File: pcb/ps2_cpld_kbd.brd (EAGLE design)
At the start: 53 x 62.2 mm, 34 parts, among them J1 AVR ISP, J2 JTAG, J3 Emulated Mechanical Keyboard, J4 Power, J5 PS/2, U1 ATMEGA328, U2 EPM7128, Y1 16MHz

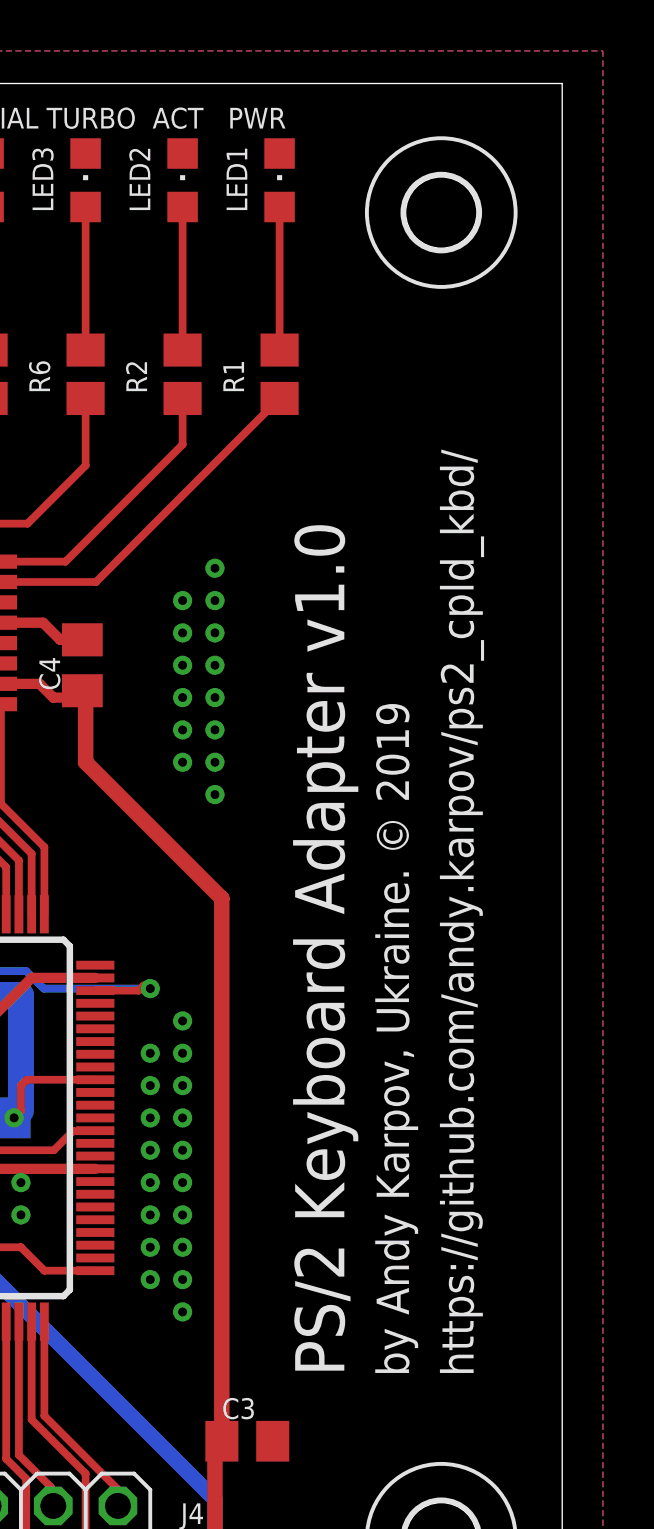
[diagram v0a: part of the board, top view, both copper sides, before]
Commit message: fixed ps/2 signal names, fixed github page url
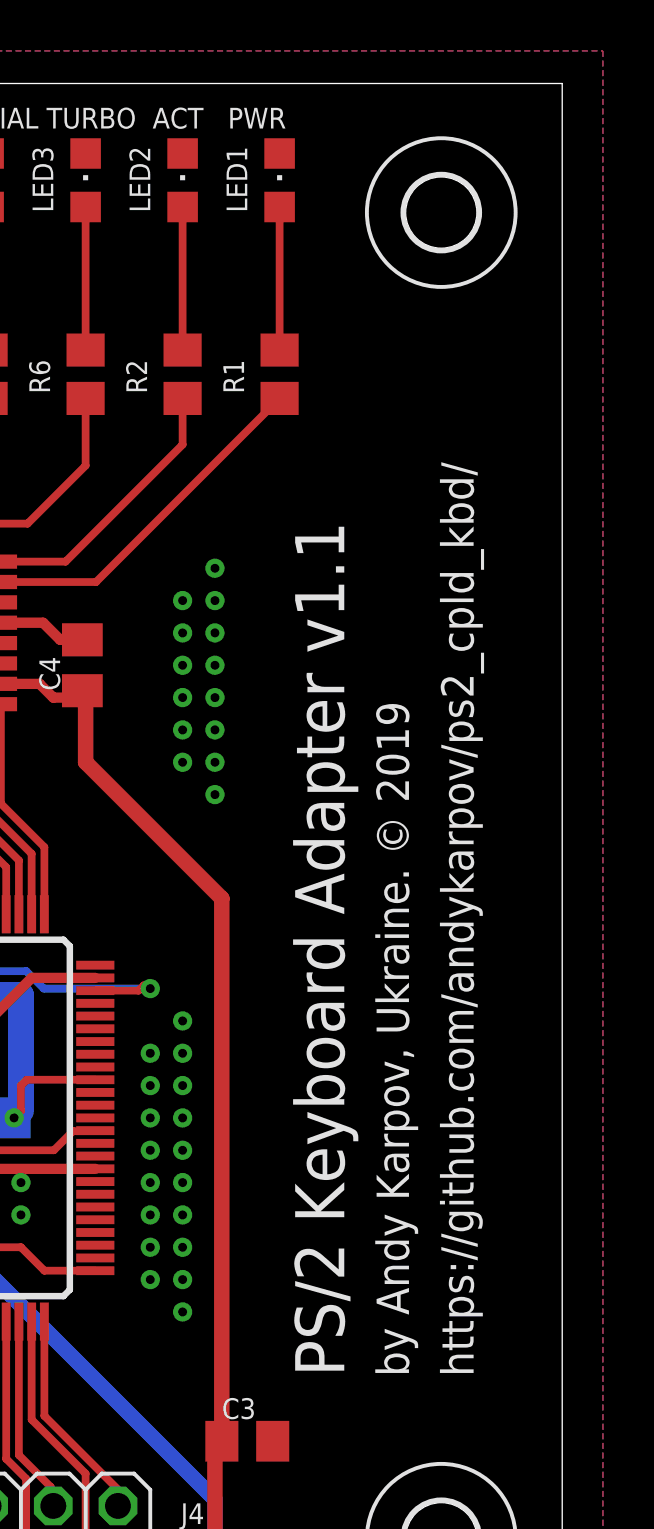
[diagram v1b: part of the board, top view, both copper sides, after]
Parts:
- J4: value Power -> VCC GND
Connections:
- net PS2_CLK: now also J5.5, R5.1, U1.1; no longer J5.1, R4.1, U1.32
- net PS2_DATA: now also J5.1, R4.1, U1.32; no longer J5.5, R5.1, U1.1
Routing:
- net PS2_DATA: track 12.8 -> 13.1 mm, vias 1 -> 0
- net PS2_CLK: track 13.1 -> 12.8 mm, vias 0 -> 1
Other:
- board text added: "PS/2 Keyboard Adapter v1.1"
- board text added: "https://github.com/andykarpov/ps2_cpld_kbd/"
- board text removed: "PS/2 Keyboard Adapter v1.0"
- board text removed: "https://github.com/andy.karpov/ps2_cpld_kbd/"
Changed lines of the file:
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@@
 <dimension x1="0" y1="0" x2="53.01" y2="0" x3="26.505" y3="-5.08" textsize="1.778" layer="20"/>
 <dimension x1="53.01" y1="0" x2="53.01" y2="62.22" x3="59.69" y3="31.11" textsize="1.778" layer="20"/>
-<text x="44.45" y="11.43" size="1.9304" layer="25" ratio="16" rot="R90">PS/2 Keyboard Adapter v1.0</text>
+<text x="44.45" y="11.43" size="1.9304" layer="25" ratio="16" rot="R90">PS/2 Keyboard Adapter v1.1</text>
 <text x="46.99" y="11.43" size="1.27" layer="25" rot="R90">by Andy Karpov, Ukraine. © 2019</text>
-<text x="49.53" y="11.43" size="1.27" layer="25" rot="R90">https://github.com/andy.karpov/ps2_cpld_kbd/</text>
+<text x="49.53" y="11.43" size="1.27" layer="25" rot="R90">https://github.com/andykarpov/ps2_cpld_kbd/</text>
 <text x="28.321" y="60.452" size="0.8128" layer="25" ratio="20">SPECIAL TURBO  ACT   PWR</text>
 <circle x="10.414" y="3.683" radius="0.508" width="0.3048" layer="25"/>
@@
 <attribute name="VALUE" x="11.43" y="1.016" size="0.8128" layer="27" ratio="20"/>
 </element>
-<element name="J4" library="pinhead" library_urn="urn:adsk.eagle:library:325" package="1X02" package3d_urn="urn:adsk.eagle:package:22435/2" value="Power" x="40.64" y="3.81" smashed="yes">
+<element name="J4" library="pinhead" library_urn="urn:adsk.eagle:library:325" package="1X02" package3d_urn="urn:adsk.eagle:package:22435/2" value="VCC GND" x="40.64" y="3.81" smashed="yes">
 <attribute name="NAME" x="38.0238" y="5.6388" size="0.8128" layer="25" ratio="10"/>
 <attribute name="VALUE" x="38.1" y="1.016" size="0.8128" layer="27" ratio="20"/>
@@
 <wire x1="22.543" y1="23.8468" x2="22.543" y2="18.181425" width="0.3048" layer="1"/>
 </signal>
-<signal name="PS2_CLK">
+<signal name="PS2_DATA">
 <contactref element="U1" pad="32"/>
 <contactref element="J5" pad="1"/>
@@
 <wire x1="18.73" y1="52.75" x2="18.73" y2="46.99" width="0.3048" layer="1"/>
 </signal>
-<signal name="PS2_DATA">
+<signal name="PS2_CLK">
 <contactref element="U1" pad="1"/>
 <contactref element="J5" pad="5"/>

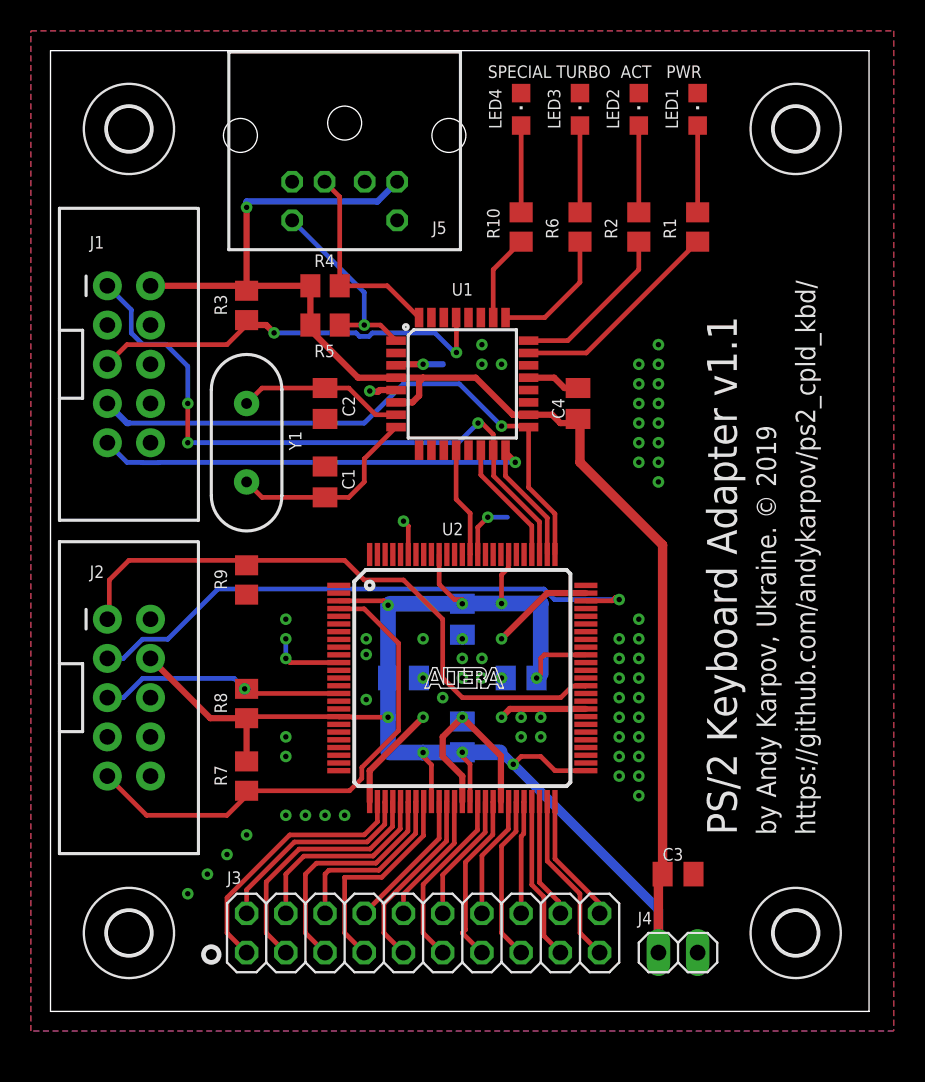
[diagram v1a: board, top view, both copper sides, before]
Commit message: updated schamatics and board v1.1
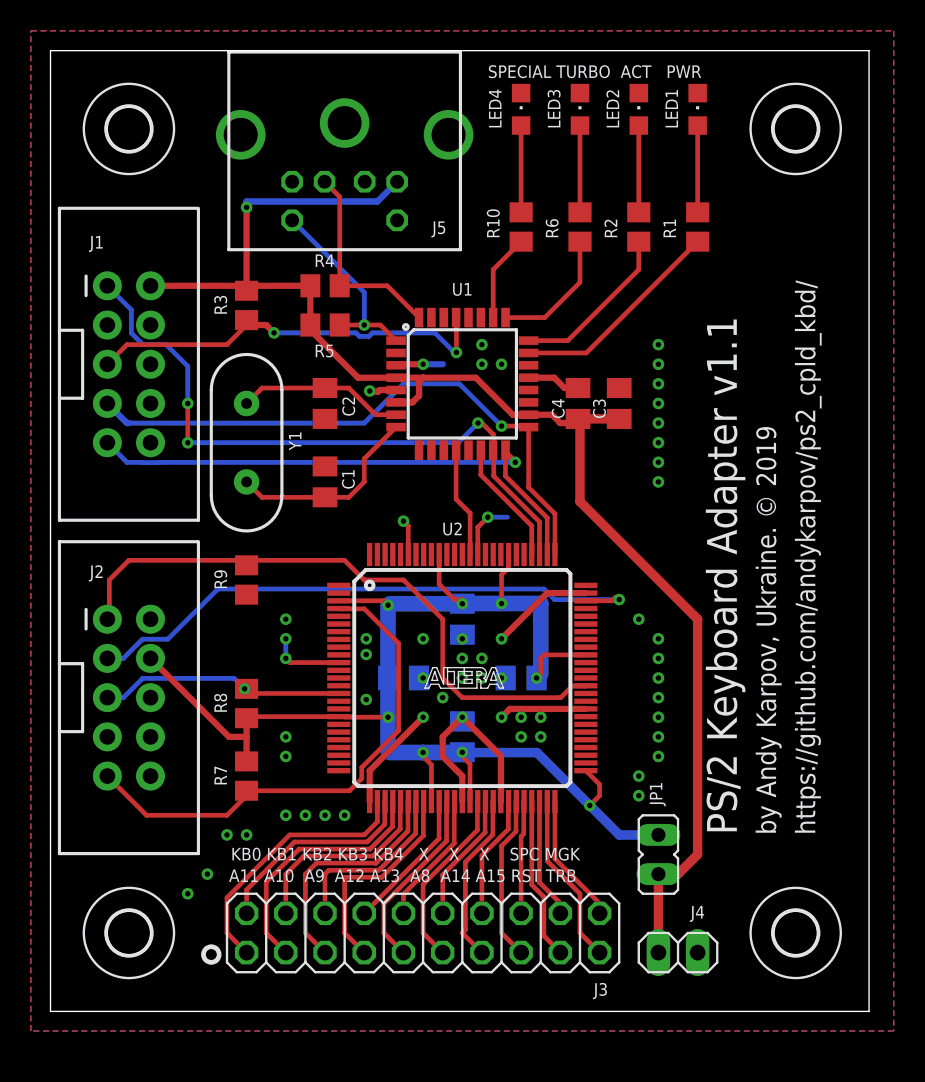
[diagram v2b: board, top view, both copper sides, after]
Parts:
- added JP1: CPLD PWR, jumper:JP1
- J5: device con-yamaichi:MDIN06SS -> con-yamaichi-mod:MDIN06SS
- moved C3 30.7 mm to (36.8, 39.4), turned to 90 degrees
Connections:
- new net VCC_CPLD: C5.1, C6.1, C7.1, C8.1, J2.4, JP1.2, R7.2, R8.2, U2.18, U2.3, U2.34, U2.39, U2.51, U2.66, U2.82, U2.91
- net GND: now also J5.GND1, J5.GND2, J5.GND3
- net VCC: now also JP1.1; no longer C5.1, C6.1, C7.1, C8.1, J2.4, R7.2, R8.2, U2.18, U2.3, U2.34, U2.39, U2.51, U2.66, U2.82, U2.91
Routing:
- net VCC: track 188.4 -> 95.1 mm, vias 9 -> 1
- net VCC_CPLD: track 0.00 -> 91.8 mm, vias 0 -> 8
- net GND: vias 72 -> 58
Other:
- board text added: "A11 A10 A9 A12 A13 A8 A14 A15 RST TRB"
- board text added: "KB0 KB1 KB2 KB3 KB4 X X X SPC MGK"

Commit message: new board v1.2 with fixes
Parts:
- added R11, R12, R13, R14, R15, R16, R17, R18: 10k, rcl:R0805
- J4: device pinhead:1X02 -> pinhead-mod:1X02
- JP1: device jumper:JP1 -> jumper-mod:JP1
- moved C3 29.3 mm to (39.4, 10.2), turned to 0 degrees
- moved R1 6.84 mm to (35.6, 53.3)
- moved H1 6.48 mm to (41.9, 3.81)
- moved H2 6.48 mm to (41.9, 58.4)
- moved LED1 6.35 mm to (35.6, 58.4)
- moved R2 5.68 mm to (33.0, 53.3)
- moved J4 5.24 mm to (35.6, 5.08), turned to 270 degrees
- moved JP1 5.24 mm to (34.3, 11.4), turned to 90 degrees
- moved LED2 5.08 mm to (33.0, 58.4)
- moved R6 4.58 mm to (30.5, 53.3)
- moved LED3 3.81 mm to (30.5, 58.4)
- moved R10 3.59 mm to (27.9, 53.3)
- moved C7 2.84 mm to (25.4, 27.9)
- moved C8 2.84 mm to (25.4, 20.3)
- moved U2 2.84 mm to (25.4, 24.1)
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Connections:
- net A10: now also R12.2
- net A11: now also R11.2
- net A12: now also R14.2
- net A13: now also R15.2
- net A14: now also R17.2
- net A15: now also R18.2
- net A8: now also R16.2
- net A9: now also R13.2
- net VCC: now also R11.1, R12.1, R13.1, R14.1, R15.1, R16.1, R17.1, R18.1
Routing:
- net VCC: track 95.1 -> 118.8 mm
- net A8: track 11.8 -> 21.3 mm
- net A15: track 10.7 -> 20.2 mm
- net A13: track 12.0 -> 21.5 mm
- net A14: track 11.1 -> 20.5 mm
- net A11: track 17.2 -> 25.4 mm
- net A12: track 13.8 -> 22.0 mm
- net A10: track 16.4 -> 24.1 mm
- net A9: track 15.3 -> 22.9 mm
- net AVR_SCK: track 39.0 -> 35.2 mm
- net AVR_MOSI: track 42.8 -> 39.4 mm
- net KB4: track 8.61 -> 11.8 mm
- net KB6: track 7.96 -> 11.0 mm
- net KB5: track 8.39 -> 11.5 mm
- net KB3: track 9.25 -> 12.3 mm
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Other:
- board size 53 x 62.2 mm -> 45.4 x 62.2 mm
- board text added: "A11 A10 A9 A12 A13 A8 A14 A15 RST TRB GND"
- board text added: "FN TURBO ACT PWR"
- board text added: "KB0 KB1 KB2 KB3 KB4 X X X SPC MGK VCC"
- board text added: "PS/2 Keyboard Adapter v1.2"
- board text removed: "A11 A10 A9 A12 A13 A8 A14 A15 RST TRB"
- board text removed: "KB0 KB1 KB2 KB3 KB4 X X X SPC MGK"
- board text removed: "PS/2 Keyboard Adapter v1.1"
- board text removed: "SPECIAL TURBO ACT PWR"
- board text removed: "by Andy Karpov, Ukraine. © 2019"
